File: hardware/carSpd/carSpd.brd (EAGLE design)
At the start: 160 x 100 mm, 78 parts, among them IC1 DS3231/SO, IC2 CP2102, Q1 2n3904, U2 MP2307, U3 7805DT, U4 ATMEGA328P_TQFP, Y1 12mhz, Y3 16mhz

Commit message: Removed the CH340G, supporting parts made it cost as much as a CP2102
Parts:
- removed C12: 10nf, rcl:C0603K
- removed C13, C14: 18pf, rcl:C0603K
- removed C15: 0.1uf, rcl:C0603K
- removed JP1: CAR_INPUT, SparkFun-Connectors:1X05
- removed U$1: CH340G, ch340g:SOIC16
- removed Y1: 12mhz, SparkFun-FreqCtrl:SMD-CYLINDER
- removed Y2: (no value), SparkFun-FreqCtrl:HC49UP
- added STANDOFF1, STANDOFF2, STANDOFF3, STANDOFF4: STAND-OFF, SparkFun-Electromechanical:STAND-OFF
- added SV1: CAR_INPUT, con-lsta:FE05W
- L1: value CD54 -> (none)
- S1, S2, S3, S4: value (none) -> SWITCH-MOMENTARY-2SMD-1101NE; device SparkFun-Electromechanical:TACTILE_SWITCH_TALL -> SparkFun-Electromechanical:TACTILE-SWITCH-1101NE
- Y3: device SparkFun-FreqCtrl:HC49UP -> SparkFun-FreqCtrl:CRYSTAL-SMD-5X3
- moved LED6 522.8 mm to (-74.3, 45.0)
- moved R18 522.8 mm to (-75.5, 39.9)
- moved U$3 522.8 mm to (-55.2, 47.6)
- moved U$4 522.8 mm to (-61.6, 47.6)
- moved U$5 522.8 mm to (-67.9, 47.6)
- moved JP3 451.3 mm to (5.99, 12.5)
- moved JP2 431.3 mm to (24.5, 7.01), turned to 270 degrees
- moved C22 428.2 mm to (-42.1, 42.5)
- moved C23 428.2 mm to (-42.1, 38.6)
- moved C24 428.2 mm to (-42.1, 34.8)
- moved C25 428.2 mm to (-42.1, 31.0)
- moved D1 428.2 mm to (-53.5, -13.4)
- moved D2 428.2 mm to (-57.3, -13.4)
- moved D3 428.2 mm to (-61.1, -13.4)
- moved LED5 428.2 mm to (-40.8, 3.09)
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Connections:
- removed net N$16: C15.1, U$1.13
- removed net N$17: C12.1, U$1.4
- removed net N$18: C14.2, U$1.8, Y1.X2, Y2.2
- removed net N$19: C13.2, U$1.7, Y1.X1, Y2.1
- net +12V: now also SV1.1; no longer JP1.1
- net +5V: no longer U$1.16
- net D+: no longer U$1.5
- net D-: no longer U$1.6
- net GND: now also S1.2, S2.2, S3.2, S4.2, SV1.5; no longer C12.2, C13.1, C14.1, JP1.5, S1.B2, S2.B2, S3.B2, S4.B2, U$1.1
- net INJ: now also SV1.3; no longer JP1.3
- net LIGHTING: now also SV1.4; no longer JP1.4
- net N$24: now also Y3.3; no longer Y3.2
- net N$28: now also S1.1; no longer S1.A2
- net N$33: now also S3.1; no longer S3.A2
- net N$34: now also S2.1; no longer S2.A2
- net N$35: now also S4.1; no longer S4.A2
- net RST: no longer C15.2
- net RX: no longer U$1.2
- net TX: no longer U$1.3
- net VSS: now also SV1.2; no longer JP1.2
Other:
- board size 160 x 100 mm -> 68.5 x 32.5 mm

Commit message: Schematic cleanup
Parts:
- removed DISP_LED: (no value), SparkFun-Connectors:1X02_NO_SILK
- removed STANDOFF1, STANDOFF2, STANDOFF3, STANDOFF4: STAND-OFF, SparkFun-Electromechanical:STAND-OFF
- removed Y3: 16mhz, SparkFun-FreqCtrl:CRYSTAL-SMD-5X3
- added Y1: 16MHZ, SparkFun-FreqCtrl:RESONATOR-SMD
- added Y2: 16mhz, SparkFun-FreqCtrl:CRYSTAL-SMD-5X3
- B1: value BATTERY1220 -> CR1220
- C17, C19, C5, C8: device rcl:C0603K -> rcl:C0805K
- C4, C7: value .1uf -> 0.1uf
- DISPLAY: value ERC1602-4 -> ERC1602-4SMD-LED; device hybridair:ERC1602-4 -> hybridair:ERC1602-4_SMDLED
- R10, R12, R13, R2, R6, R9: device rcl:R0603 -> rcl:R0805
- R14: value 220 -> 270
- R15, R16, R17: value 50k -> 47k; device rcl:R0603 -> rcl:R0805
- R18: value 1k -> 2.7k
- R8: value 220 -> 150
- S1, S2, S3, S4: value SWITCH-MOMENTARY-2SMD-1101NE -> (none)
- moved LED4 160.4 mm to (61.2, 30.1)
- moved LED3 132.7 mm to (39.5, 30.1)
- moved LED2 115.9 mm to (28.9, 30.1)
- moved LED1 88.5 mm to (7.23, 30.1)
- moved IC1 29.1 mm to (25.4, 19.4), turned to 90 degrees
- moved JP3 9.06 mm to (6.01, 21.5), flipped to the bottom, turned to 180 degrees
- moved S5 9.06 mm to (4.74, 11.7), flipped to the bottom
- moved SV1 6.00 mm to (40.0, 5.00), flipped to the bottom
- moved IC2 5.66 mm to (16.1, 19.9), flipped to the bottom
- moved B1 2.00 mm to (56.1, 24.9), flipped to the bottom
- moved S1 2.00 mm to (13.0, 30.0)
- moved S2 2.00 mm to (23.0, 30.0)
- moved S3 2.00 mm to (45.0, 30.0)
- moved S4 2.00 mm to (55.0, 30.0)
- moved U3 1.30 mm to (52.9, 11.4), flipped to the bottom, turned to 90 degrees
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- renumbered U$3 to D4, U$4 to D5, U$5 to D6
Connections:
- removed net N$13: DISP_LED.2, R8.1
- new net N$16: DISPLAY.LED+, R8.1
- net GND: now also C23.1, DISPLAY.LED-, Y1.2; no longer C23.2, DISP_LED.1
- net N$24: now also Y1.1, Y2.3; no longer Y3.3
- net N$37: now also C23.2, Y1.3, Y2.1; no longer C23.1, Y3.1

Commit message: Modified and added parts list
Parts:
- C6: value .33uf -> 100uf; device rcl:C0603K -> ELL-i-Passives:CPOL_PANASONIC_D
- C7: value 0.1uf -> 10uf
- moved C6 123.2 mm to (51.0, 4.00), flipped to the bottom
- moved U3 1.00 mm to (52.9, 12.4)
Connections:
- net +12V: now also C6.+; no longer C6.1
- net GND: now also C6.-; no longer C6.2

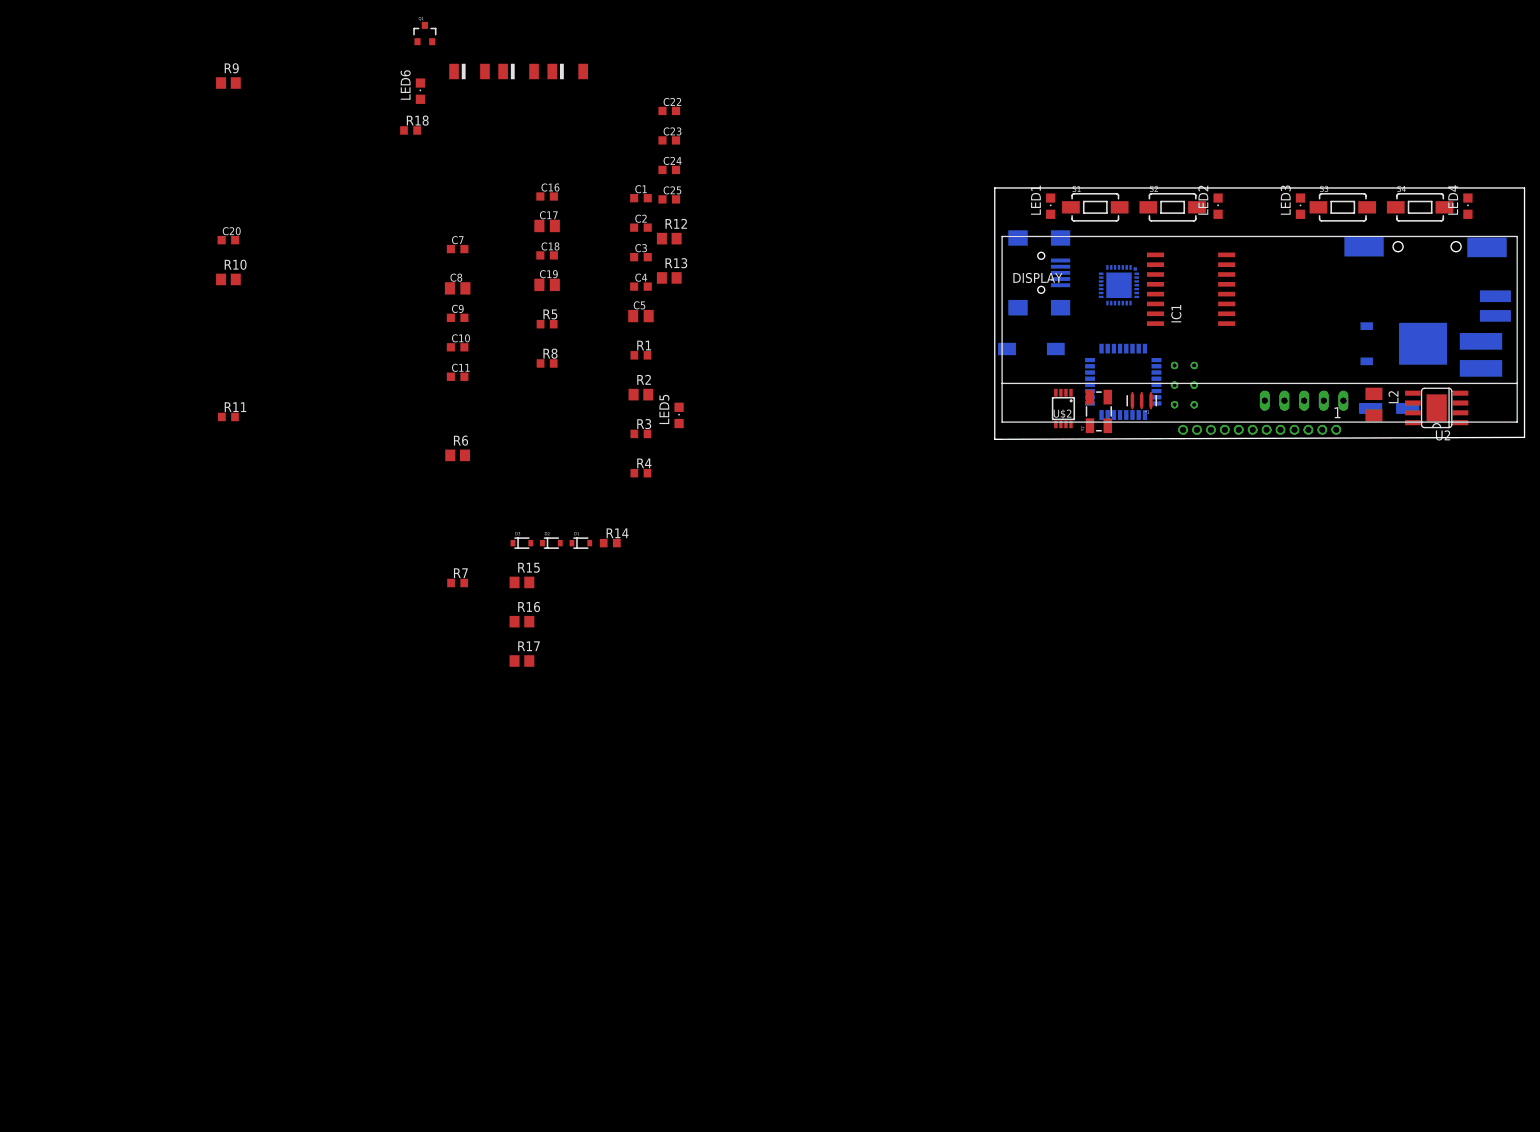
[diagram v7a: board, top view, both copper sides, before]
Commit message: Replaced power regulator circuits
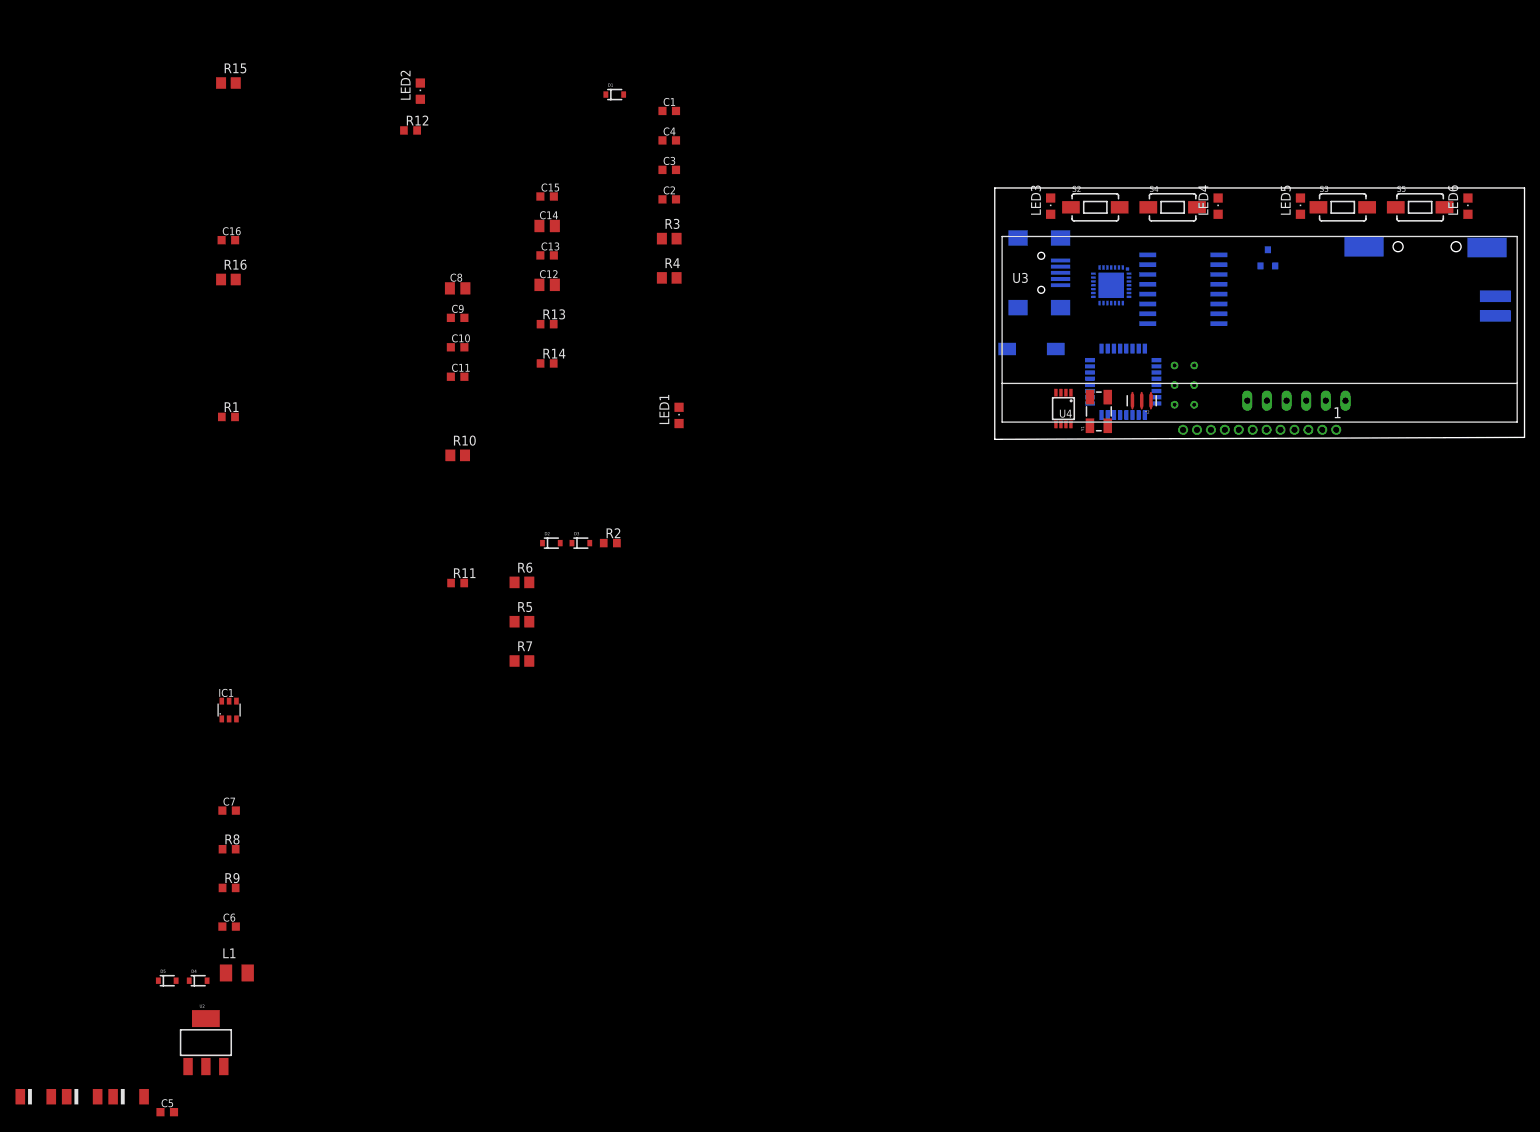
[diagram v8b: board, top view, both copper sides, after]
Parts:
- removed C20, C24, C25: 0.1uf, rcl:C0603K
- removed C22, C23: 18pf, rcl:C0603K
- removed DISPLAY: ERC1602-4SMD-LED, hybridair:ERC1602-4_SMDLED
- removed JP3: USBSMD, SparkFun-Connectors:USB-MINIB
- removed L2: 10uh, rcl:L3225M
- removed R17: 47k, rcl:R0805
- removed R18: 2.7k, rcl:R0603
- removed U$2: DS1820, Ava:µSOP8
- added C15: 0.1uf, rcl:C0603K
- added D7, D8: ZMM5V1, hybridair:SOD-80
- added IC3: DS3231/SO, adafruit:SO16W
- added JP1: AVR_ICSP, SparkFun-Connectors:2X3_TEST_POINTS
- added U1: ATMEGA328P_TQFP, SparkFun-DigitalIC:TQFP32-08
- C1: value 10uf -> 18pf
- C2: value 22uf -> 0.1uf
- C3: value 3.9nf -> 0.1uf
- C4: value 0.1uf -> 18pf
- C5: value 10nf -> 10uf; device rcl:C0805K -> rcl:C0603K
- C6: value 100uf -> 100nf; device ELL-i-Passives:CPOL_PANASONIC_D -> rcl:C0603K
- C7: value 10uf -> 22uf
- D4: value 5.1V -> (none); device hybridair:SOD-80 -> SparkFun-DiscreteSemi:SOD-323
- D5: value 5.1V -> 1N4148; device hybridair:SOD-80 -> SparkFun-DiscreteSemi:SOD-323
- D6: value 5.1V -> ZMM5V1
- IC1: value DS3231/SO -> MCP16301/H; device adafruit:SO16W -> MCP16301:SOT23-6
- JP2: value AVR_ICSP -> USBSMD; device SparkFun-Connectors:2X3_TEST_POINTS -> SparkFun-Connectors:USB-MINIB
- L1: value (none) -> 22uh; device inductor-sumida:CD54 -> rcl:L3225M
- LED1: value (none) -> STATUS
- LED2: value (none) -> POWER
- LED5: value STATUS -> (none)
- LED6: value POWER -> (none)
- R12: value 4.7k -> 2.7k; device rcl:R0805 -> rcl:R0603
- R13: value 4.7k -> 10k; device rcl:R0805 -> rcl:R0603
- R14: value 270 -> 150
- R15, R16: value 47k -> 4.7k
- R2: value 100k -> 270; device rcl:R0805 -> rcl:R0603
- R3: value 6.8k -> 4.7k; device rcl:R0603 -> rcl:R0805
- R4: value 44.2k -> 4.7k; device rcl:R0603 -> rcl:R0805
- R5, R7: value 10k -> 47k; device rcl:R0603 -> rcl:R0805
- R6: value 4.7k -> 47k
- R8: value 150 -> 10k
- R9: value 4.7k -> 52.3k; device rcl:R0805 -> rcl:R0603
- S1: value (none) -> RESET
- S5: value RESET -> (none)
- SV1: device con-lsta:FE05W -> con-lsta:FE06W
- U2: value MP2307 -> (none); device hybridair:SOIC8 -> SparkFun-IC-Power:SOT223
- U3: value 7805DT -> ERC1602-4SMD-LED; device adafruit:TO252 -> hybridair:ERC1602-4_SMDLED
- U4: value ATMEGA328P_TQFP -> DS1820; device SparkFun-DigitalIC:TQFP32-08 -> Ava:µSOP8
- Y1: value 16MHZ -> 16mhz; device SparkFun-FreqCtrl:RESONATOR-SMD -> SparkFun-FreqCtrl:CRYSTAL-SMD-5X3
- Y2: value 16mhz -> 16MHZ; device SparkFun-FreqCtrl:CRYSTAL-SMD-5X3 -> SparkFun-FreqCtrl:RESONATOR-SMD
- moved L1 179.6 mm to (-98.0, -69.0), flipped to the top
- moved U2 179.1 mm to (-102.0, -78.0), turned to 0 degrees
- moved C6 164.3 mm to (-99.0, -63.0), flipped to the top
- moved D6 139.7 mm to (-112.0, -85.0)
- moved LED6 136.3 mm to (61.2, 30.1)
- moved IC1 135.8 mm to (-99.0, -35.0), turned to 0 degrees
- moved D4 126.9 mm to (-103.0, -70.0)
- moved D5 126.0 mm to (-107.0, -70.0)
- moved C5 119.8 mm to (-107.0, -87.0)
- moved Q1 112.8 mm to (35.3, 23.4), flipped to the bottom
- moved LED2 104.2 mm to (-74.3, 45.0)
- moved R9 104.1 mm to (-99.0, -58.0)
- moved LED5 84.8 mm to (39.5, 30.1)
- moved C7 78.4 mm to (-99.0, -48.0)
- moved R8 75.1 mm to (-99.0, -53.0)
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- renumbered C17 to C14, C18 to C13, C19 to C12
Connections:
- removed net N$1: C5.2, U2.1
- removed net N$2: C5.1, L1.2, L2.2, U2.3
- removed net N$3: R1.2, R4.2, U2.5
- removed net N$5: C3.2, R3.2
- removed net N$6: C3.1, U2.6
- removed net N$7: C4.1, U2.8
- removed net N$9: R2.1, U2.7
- new net N$18: C6.1, D4.C, IC1.6, L1.1
- new net N$19: C6.2, D5.C, IC1.1
- new net N$25: C7.2, IC1.3, R8.1, R9.1
- net +12V: now also C5.1, IC1.4, IC1.5, SV1.2, U2.3; no longer C1.1, C6.+, R2.2, SV1.1, U2.2, U3.1
- net +5V: now also C15.1, C3.1, D5.A, IC3.2, JP1.2, JP2.VBUS, L1.2, R1.1, R12.2, R16.2, R3.1, R9.2, SV1.1, U1.18, U1.4, U1.6, U2.2, U2.4, U3.1, U3.7, U3.9, U4.8; no longer C20.1, C24.1, C25.1, DISPLAY.1, DISPLAY.2, DISPLAY.7, DISPLAY.9, IC1.2, JP2.2, JP3.VBUS, L1.1, L2.1, R11.1, R12.1, R13.1, R18.2, R6.2, U$2.8, U4.18, U4.4, U4.6
- net D+: now also JP2.D+; no longer JP3.D+
- net D-: now also JP2.D-; no longer JP3.D-
- net GND: now also C15.2, C3.2, C4.1, C5.2, D7.A, D8.A, IC1.2, IC3.10, IC3.11, IC3.12, IC3.13, IC3.5, IC3.6, IC3.7, IC3.8, IC3.9, JP1.6, JP2.GND, LED5.C, R11.1, R2.2, R8.2, S1.1, S5.2, SV1.6, U1.21, U1.3, U1.5, U2.1, U3.10, U3.6, U3.LED-, U4.4, Y2.2; no longer C20.2, C22.2, C23.1, C24.2, C25.2, C4.2, C6.-, C7.2, D5.A, DISPLAY.10, DISPLAY.3, DISPLAY.6, DISPLAY.LED-, IC1.10, IC1.11, IC1.12, IC1.13, IC1.5, IC1.6, IC1.7, IC1.8, IC1.9, JP2.6, JP3.GND, LED1.C, R1.1, R14.2, R3.1, R7.1, S1.2, S5.1, SV1.5, U$2.4, U2.4, U2.P$1, U4.21, U4.3, U4.5, Y1.2
- net INJ: now also R6.1, SV1.4; no longer R15.1, SV1.3
- net LED_PWM: now also JP1.4, R13.2, U1.15; no longer JP2.4, R5.2, U4.15
- net LIGHTING: now also R7.1, SV1.5; no longer R17.1, SV1.4
- net N$11: now also R13.1; no longer R5.1
- net N$14: now also U3.8; no longer DISPLAY.8
- net N$15: now also R14.2, R15.2; no longer R8.2, R9.2
- net N$16: now also R14.1, U3.LED+; no longer DISPLAY.LED+, R8.1
- net N$20: now also U3.11; no longer DISPLAY.11
- net N$21: now also U3.12; no longer DISPLAY.12
- net N$22: now also JP1.1, U1.16; no longer JP2.1, U4.16
- net N$23: now also LED5.A, LED6.A, R15.1; no longer LED1.A, LED2.A, R9.1
- net N$24: now also C1.1, U1.7, Y1.3, Y2.1; no longer C22.1, U4.7, Y1.1, Y2.3
- net N$26: now also JP1.3, LED1.A, U1.17; no longer JP2.3, LED5.A, U4.17
- net N$27: now also IC3.14; no longer IC1.14
- net N$28: now also S2.1, U1.10; no longer S1.1, U4.10
- net N$29: now also LED2.A, R12.1; no longer LED6.A, R18.1
- net N$30: now also D7.C, R6.2, U1.1, U1.32; no longer D5.C, R15.2, U4.1, U4.32
- net N$31: now also D3.C, D8.C, R7.2, U1.23; no longer D1.C, D4.C, R17.2, U4.23
- net N$32: now also LED1.C, R2.1; no longer LED5.C, R14.1
- net N$33: now also U1.12; no longer U4.12
- net N$34: now also S4.1, U1.11; no longer S2.1, U4.11
- net N$35: now also S5.1, U1.13; no longer S4.1, U4.13
- net N$36: now also D1.C, R5.2, U1.9; no longer D3.C, R16.2, U4.9
- net N$37: now also C4.2, U1.8, Y1.1, Y2.3; no longer C23.2, U4.8, Y1.3, Y2.1
- net N$4: now also R10.1; no longer R6.1
- net N$8: now also R11.2; no longer R7.2
- net RST: now also JP1.5, R1.2, S1.2, U1.29; no longer JP2.5, R11.2, S5.2, U4.29
- net RX: now also U1.30; no longer U4.30
- net SCL: now also IC3.16, R4.2, U1.28, U3.4; no longer DISPLAY.4, IC1.16, R13.2, U4.28
- net SDA: now also IC3.15, R3.2, U1.27, U3.5; no longer DISPLAY.5, IC1.15, R12.2, U4.27
- net TEMP: now also R16.1, U4.1; no longer R10.1, U$2.1
- net TX: now also U1.31; no longer U4.31
- net VSS: now also R5.1, SV1.3; no longer R16.1, SV1.2
